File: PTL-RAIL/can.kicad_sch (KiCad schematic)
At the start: 0 parts

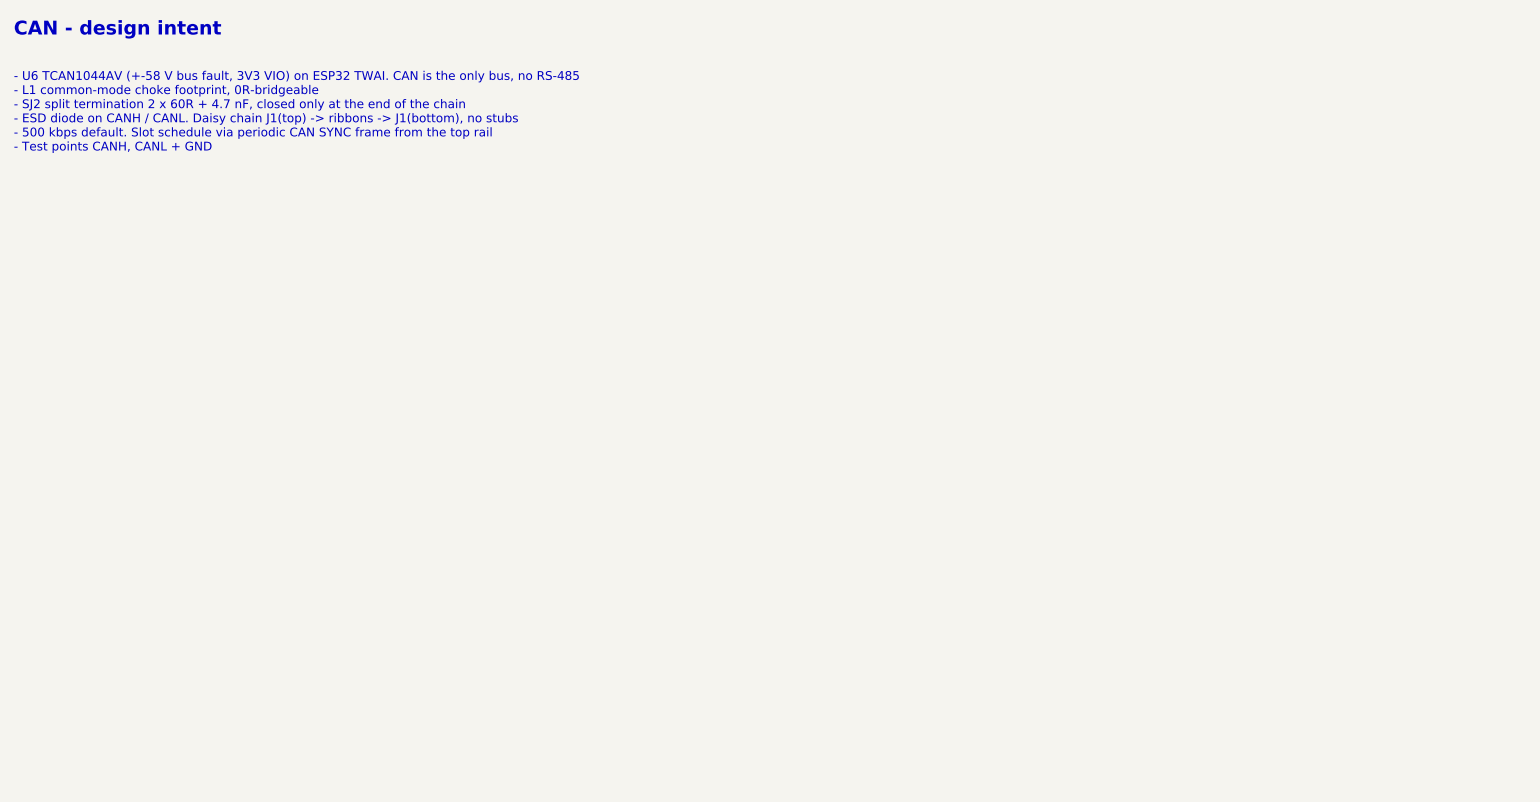
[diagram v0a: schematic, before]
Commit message: PTL-RAIL: LED row on top edge, TSOP row on bottom edge, node parts aligned at 84 mm pitch; J3/J4 10-way and J5/J6 4-way screw terminals
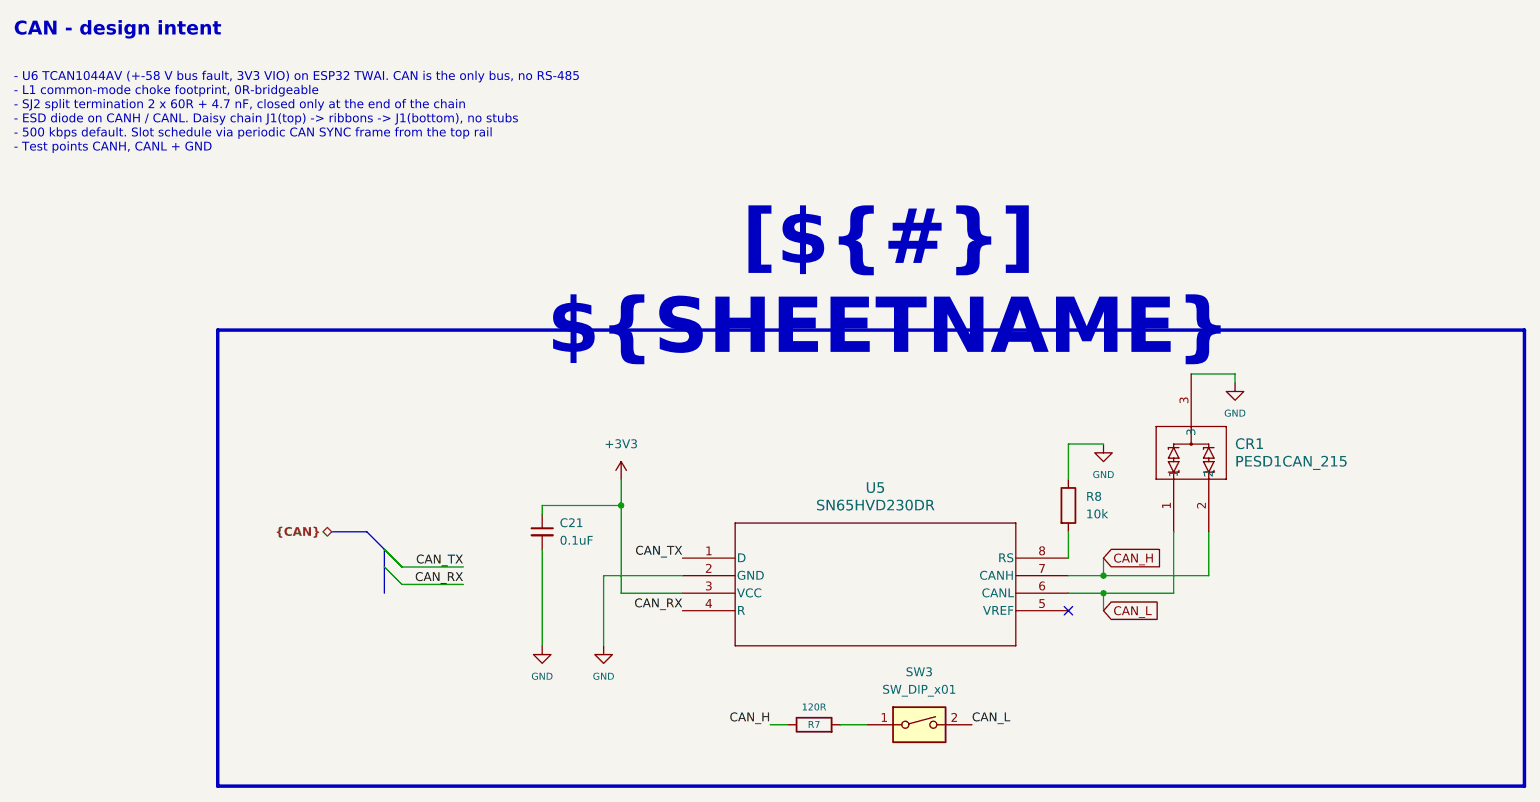
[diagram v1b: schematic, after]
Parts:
- added C21: 0.1uF, Capacitor_SMD:C_0805_2012Metric, symbol Device:C_Small
- added CR1: PESD1CAN_215, Package_TO_SOT_SMD:SOT-23, symbol 0_PESD1CAN:PESD1CAN_215
- added R7: 120R, Resistor_SMD:R_0805_2012Metric, symbol Device:R
- added R8: 10k, Resistor_SMD:R_0805_2012Metric, symbol Device:R
- added SW3: SW_DIP_x01, Button_Switch_THT:SW_DIP_SPSTx01_Slide_9.78x4.72mm_W7.62mm_P2.54mm, symbol Switch:SW_DIP_x01
- added U5: SN65HVD230DR, Package_SO:SOIC-8_3.9x4.9mm_P1.27mm, symbol 0_SN65HVD230DR:SN65HVD230DR
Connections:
- new net: R8.2, U5.8 (RS)
- new net: R7.2, SW3.1
- new net +3V3: C21.1, U5.3 (VCC)
- new net CAN_H: CR1.2, R7.1, U5.7 (CANH)
- new net CAN_L: CR1.1, SW3.2, U5.6 (CANL)
- new net CAN_RX: U5.4 (R)
- new net CAN_TX: U5.1 (D)
- new net GND: C21.2, CR1.3, R8.1, U5.2 (GND)
- no-connect marks 0 -> 1

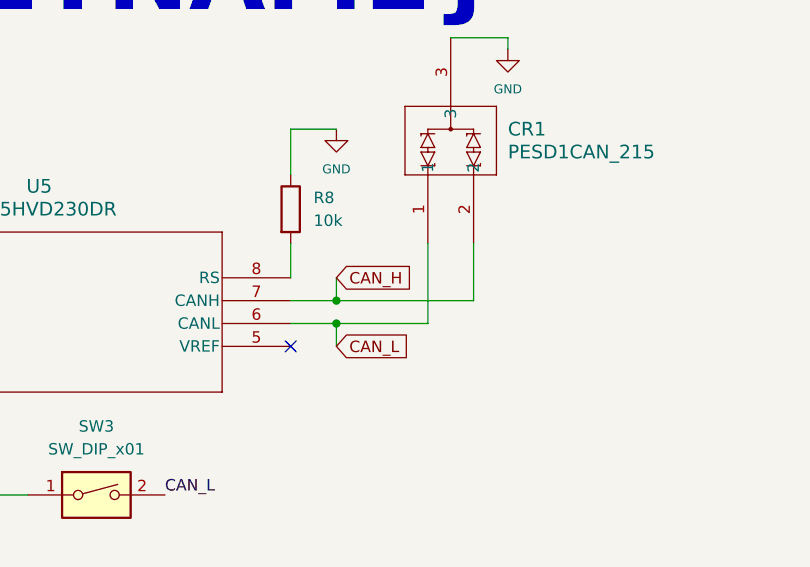
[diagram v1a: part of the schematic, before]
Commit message: PTL-RAIL: IR shrouds, bottom-side node parts, test points, SW4 user button
- 3D-printed shroud outlines (28 mm) with M3 mounting holes on every LED
  and TSOP node, replicated from node 2; parts cleared from shroud areas
- TX/RX node resistors, caps and MOSFETs moved to the bottom layer and
  arranged uniformly per node
- Filleted the TSOP output bus corners; solid zone connection on the
  starved-thermal GND pads
- Silkscreen cleanup: uniform 0.8 mm refs, connector pin labels on both
  sides, J5/J6 mirrored labels, node TX/RX labels, title/company/date
- Redundant GND vias and a GND via fence along the board edge
- Mid-board mounting holes (H25-H28) and 4 mm rounded corners concentric
  with the corner holes
- Test points TP5-TP19 (TX_1-5, TSOP_OUT_1-5, VIN, +5V, +3V3, 2x GND)
  in schematic and PCB, routed
- SW4 generic user push button with R34 10k pull-up
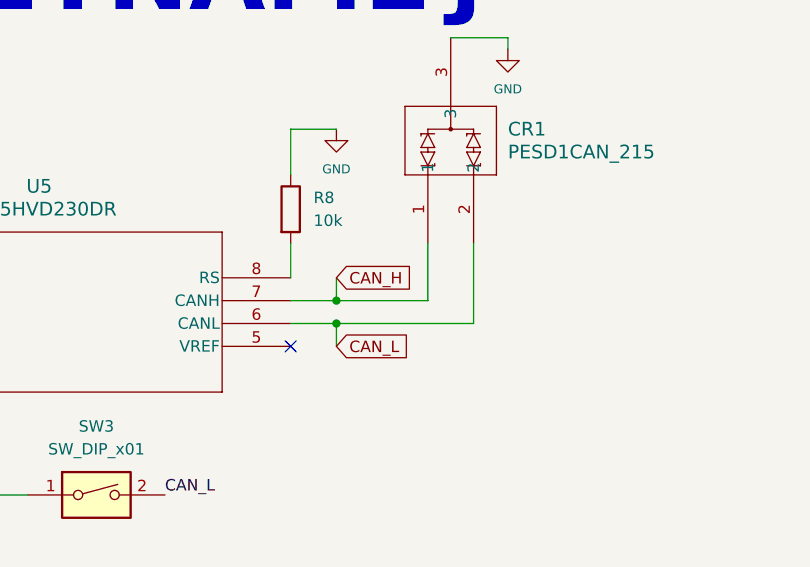
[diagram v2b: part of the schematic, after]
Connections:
- net CAN_H: now also CR1.1; no longer CR1.2
- net CAN_L: now also CR1.2; no longer CR1.1
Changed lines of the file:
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@@
+	(wire
+		(pts
+			(xy 187.96 102.87) (xy 177.8 102.87)
+		)
+		(stroke
+			(width 0)
+			(type default)
+		)
+	)
 	(wire
 		(pts
@@
 	(wire
 		(pts
-			(xy 187.96 96.52) (xy 187.96 105.41)
-		)
-		(stroke
-			(width 0)
-			(type default)
-		)
-	)
-	(wire
-		(pts
 			(xy 177.8 100.33) (xy 177.8 102.87)
 		)
@@
 	(wire
 		(pts
-			(xy 177.8 105.41) (xy 187.96 105.41)
+			(xy 177.8 105.41) (xy 193.04 105.41)
 		)
 		(stroke
@@
 	(wire
 		(pts
-			(xy 193.04 96.52) (xy 193.04 102.87)
+			(xy 187.96 96.52) (xy 187.96 102.87)
 		)
 		(stroke
@@
 	(wire
 		(pts
+			(xy 193.04 96.52) (xy 193.04 105.41)
+		)
+		(stroke
+			(width 0)
+			(type default)
+		)
+	)
+	(wire
+		(pts
 			(xy 172.72 96.52) (xy 172.72 100.33)
 		)
@@
 		)
 		(stroke
-			(width 0)
-			(type default)
-		)
-	)
-	(wire
-		(pts
-			(xy 177.8 102.87) (xy 193.04 102.87)
-		)
-		(stroke

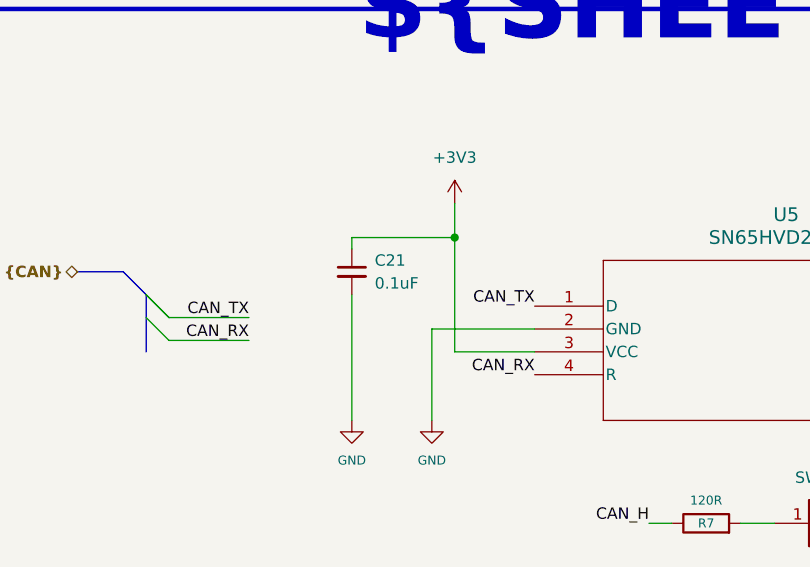
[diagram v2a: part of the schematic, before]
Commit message: PTL-RAIL rev A: normalize cap values, IO45 no-connect, README and docs
- Capacitor values unified: 0.1uF -> 100nF (C10, C16-C21, C27; now one
  BOM line with C5), '4.7 µF' -> 4.7uF (C22-C26)
- No-connect flag on U3 IO45 (ERC clean apart from 2 CAN label warnings)
- Zones refilled
- PTL-RAIL/README.md: board summary, pinouts, ESP32 pin map, test points,
  mounting, fab/assembly notes, production file list, rev A open issues
- Root README points to PTL-RAIL and the release assets
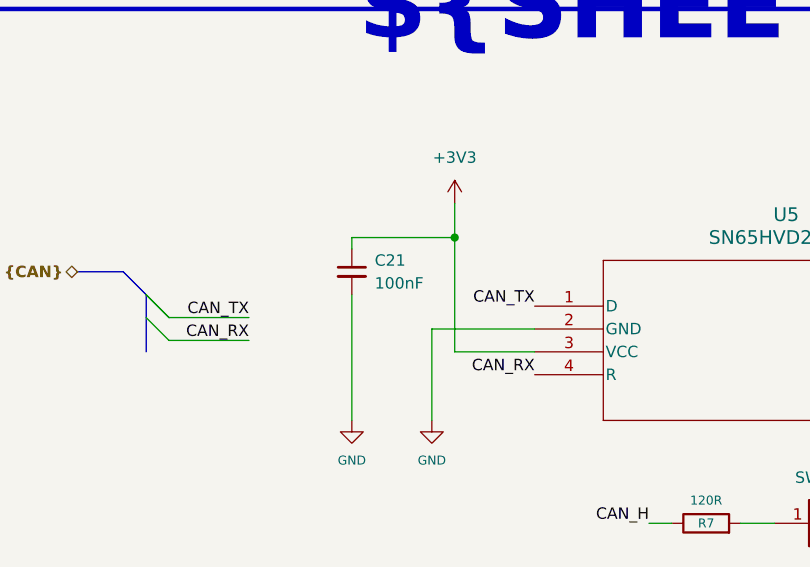
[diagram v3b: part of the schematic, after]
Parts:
- C21: value 0.1uF -> 100nF
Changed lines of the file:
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@@
 			)
 		)
-		(property "Value" "0.1uF"
+		(property "Value" "100nF"
 			(at 99.06 97.7962 0)
 			(show_name no)
